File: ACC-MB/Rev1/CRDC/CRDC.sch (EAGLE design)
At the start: 7 parts

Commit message: update
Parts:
- removed U$5: TO247RESISTORHEATINK, ACC-MB-R0:TO247RESISTORHEATINK
- added LED1, LED2: (no value), ACC-MB-R0:LED3MM
- added R1, R2: (no value), ACC-MB-R0:RMG100-H
- added R3, R4: (no value), ACC-MB-R0:R-US_R0805
- added U$8, U$9: HEATSINK40X40X15, ACC-MB-R0:HEATSINK40X40X15
- U$3: value TO247RESISTORHEATINK -> BENDER_IRR155; device ACC-MB-R0:TO247RESISTORHEATINK -> ACC-MB-R0:BENDER_IRR155
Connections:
- net HV-_DRY renamed HV-_DRY_AUX
- new net N$1: LED2.C, R3.2
- new net N$5: LED1.C, R4.2
- net DISCHARGE: now also LED2.A
- net GND: now also R3.1, R4.1
- net HV+_DRY: now also R2.1; no longer U$3.P$2
- net HV+_WET: now also R1.1; no longer U$5.P$2
- net N$21: now also R1.2; no longer U$5.P$1
- net N$4: now also R2.2; no longer U$3.P$1
- net PRECHARGE: now also LED1.A

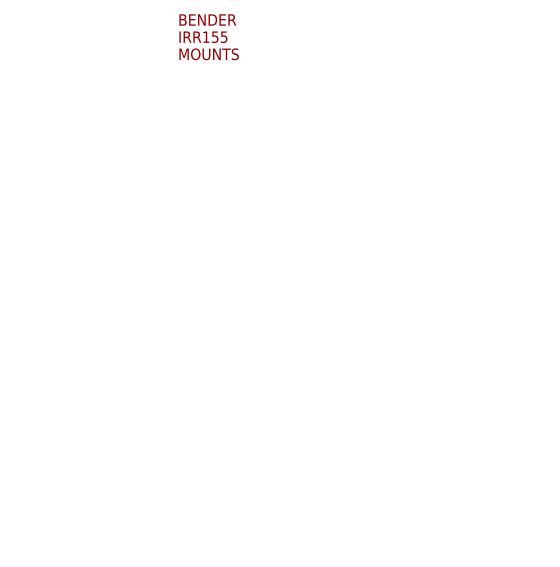
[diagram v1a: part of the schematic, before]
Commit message: 7792 added to all DC
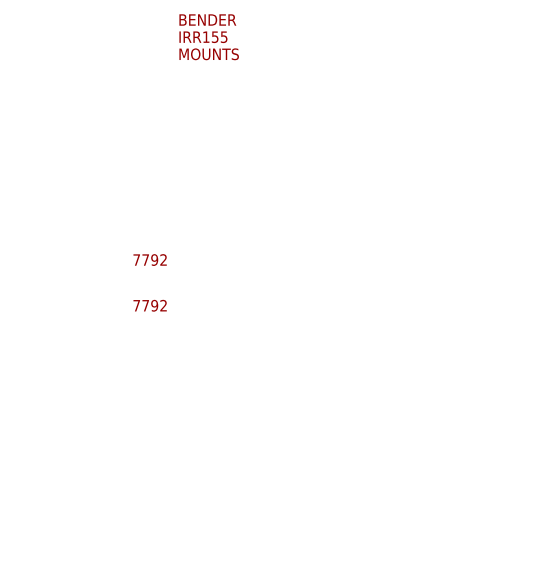
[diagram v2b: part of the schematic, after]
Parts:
- added U$10, U$5: 7792, ACC-MB-R0:7792
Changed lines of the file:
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@@
 <part name="GND6" library="ACC-MB-R0" library_urn="urn:adsk.eagle:library:13208985" deviceset="GND" device=""/>
 <part name="U$3" library="ACC-MB-R0" library_urn="urn:adsk.eagle:library:13208985" deviceset="BENDER_IRR155" device="" package3d_urn="urn:adsk.eagle:package:14400200/2"/>
+<part name="U$5" library="ACC-MB-R0" library_urn="urn:adsk.eagle:library:13208985" deviceset="7792" device="" package3d_urn="urn:adsk.eagle:package:14511284/2"/>
+<part name="U$10" library="ACC-MB-R0" library_urn="urn:adsk.eagle:library:13208985" deviceset="7792" device="" package3d_urn="urn:adsk.eagle:package:14511284/2"/>
 </parts>
 <sheets>
@@
 <instance part="GND6" gate="1" x="213.36" y="138.43"/>
 <instance part="U$3" gate="G$1" x="22.86" y="200.66"/>
+<instance part="U$5" gate="G$1" x="17.78" y="177.8"/>
+<instance part="U$10" gate="G$1" x="17.78" y="172.72"/>
 </instances>
 <busses>
